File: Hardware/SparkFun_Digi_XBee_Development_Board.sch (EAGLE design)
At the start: 80 parts, among them J4 QWIIC_RIGHT_ANGLE, Q2 3.1A/30V/105mΩ, U1 FSUSB30MUX_MSOP10, U2 AP63203, U3 ESD Diode, U4 MCP73831, U5 ESD Diode, U7 FT231XS

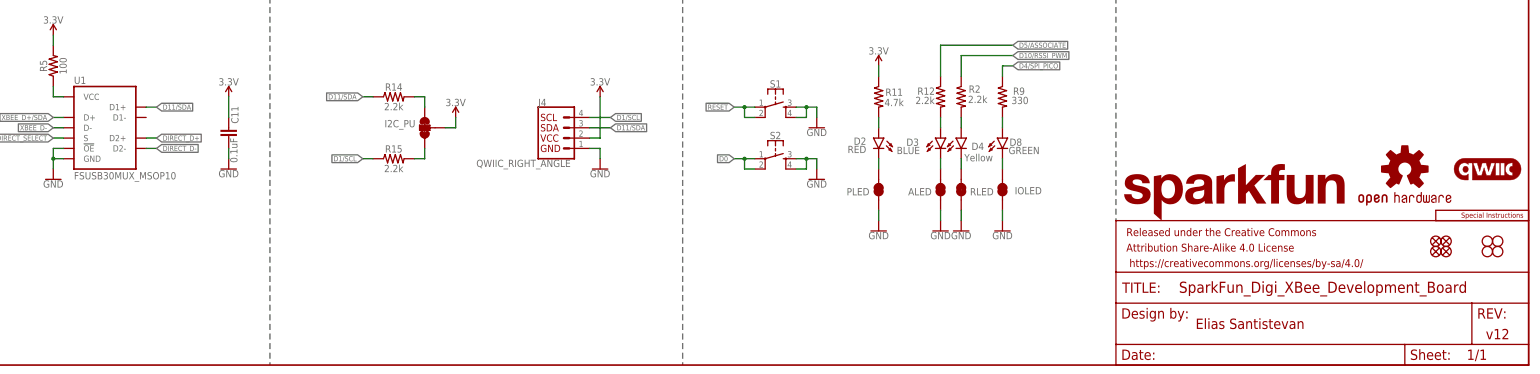
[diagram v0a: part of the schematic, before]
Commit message: Adds new FSUSB42 MUX switch
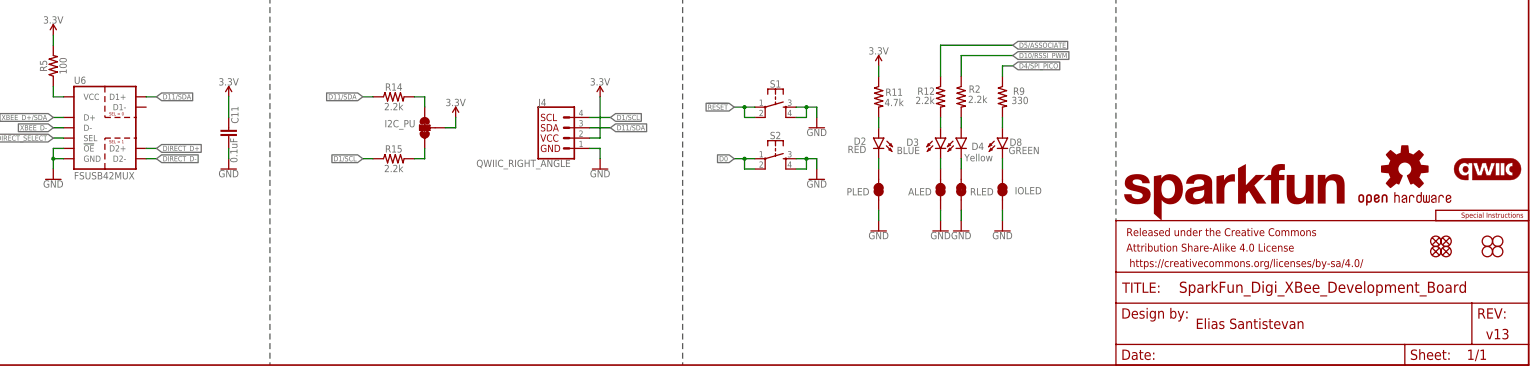
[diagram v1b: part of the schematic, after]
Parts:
- removed U1: FSUSB30MUX_MSOP10, SparkFun-IC-Special-Function:FSUSB30MUX_MSOP10
- added U6: FSUSB42MUX, SparkFun-IC-Special-Function:FSUSB42MUX
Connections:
- net D11/SDA: now also U6.D1+; no longer U1.D1+
- net DIRECT_D+: now also U6.D2+; no longer U1.D2+
- net DIRECT_D-: now also U6.D2-; no longer U1.D2-
- net DIRECT_SELECT: now also U6.SEL; no longer U1.S
- net GND: now also U6.!OE!, U6.GND; no longer U1.!OE!, U1.GND
- net N$3: now also U6.VCC; no longer U1.VCC
- net XBEE_D+/SDA: now also U6.D+; no longer U1.D+
- net XBEE_D-: now also U6.D-; no longer U1.D-
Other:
- note added: "v13"
- note removed: "v12"
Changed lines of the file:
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@@
 <part name="R12" library="SparkFun-Resistors" deviceset="2.2KOHM" device="-0603-1/10W-1%" value="2.2k"/>
 <part name="GND14" library="SparkFun-PowerSymbols" deviceset="GND" device=""/>
-<part name="U1" library="SparkFun-IC-Special-Function" deviceset="FSUSB30MUX" device="_MSOP10"/>
 <part name="GND22" library="SparkFun-PowerSymbols" deviceset="GND" device=""/>
 <part name="SUPPLY10" library="SparkFun-PowerSymbols" deviceset="3.3V" device=""/>
@@
 <part name="SUPPLY22" library="SparkFun-PowerSymbols" deviceset="V_USB" device=""/>
 <part name="SUPPLY6" library="SparkFun-PowerSymbols" deviceset="V_USB" device=""/>
+<part name="U6" library="SparkFun-IC-Special-Function" deviceset="FSUSB42MUX" device=""/>
 </parts>
 <sheets>
@@
 <wire x1="294.64" y1="187.96" x2="431.8" y2="187.96" width="0.2032" layer="97" style="longdash"/>
 <wire x1="121.92" y1="111.76" x2="121.92" y2="0" width="0.2032" layer="97" style="longdash"/>
-<text x="424.18" y="7.62" size="2.54" layer="94" font="vector" align="center">v12</text>
+<text x="424.18" y="7.62" size="2.54" layer="94" font="vector" align="center">v13</text>
 <text x="363.22" y="10.16" size="2.54" layer="94" font="vector" align="center">Elias Santistevan</text>
 <wire x1="223.52" y1="111.76" x2="223.52" y2="0" width="0.2032" layer="97" style="longdash"/>
@@
 <attribute name="VALUE" x="287.02" y="32.766" size="1.778" layer="96" font="vector" align="top-center"/>
 </instance>
-<instance part="U1" gate="U1" x="81.28" y="58.42" smashed="yes">
-<attribute name="NAME" x="73.66" y="69.215" size="1.778" layer="95" font="vector"/>
-<attribute name="VALUE" x="73.66" y="45.72" size="1.778" layer="96" font="vector"/>
-</instance>
 <instance part="GND22" gate="1" x="17.78" y="210.82" smashed="yes" rot="MR0">
 <attribute name="VALUE" x="17.78" y="210.566" size="1.778" layer="96" font="vector" rot="MR0" align="top-center"/>
@@
 <attribute name="VALUE" x="353.06" y="246.634" size="1.778" layer="96" font="vector" align="bottom-center"/>
 </instance>
+<instance part="U6" gate="G$1" x="81.28" y="58.42" smashed="yes">
+<attribute name="NAME" x="73.66" y="69.215" size="1.778" layer="95" font="vector"/>
+<attribute name="VALUE" x="73.66" y="45.72" size="1.778" layer="96" font="vector"/>
+</instance>
 </instances>
 <busses>
@@
 </segment>
 <segment>
-<pinref part="U1" gate="U1" pin="D1+"/>
-<wire x1="93.98" y1="63.5" x2="91.44" y2="63.5" width="0.1524" layer="91"/>
-<label x="93.98" y="63.5" size="1.27" layer="95" font="vector" xref="yes"/>
+<wire x1="93.98" y1="66.04" x2="91.44" y2="66.04" width="0.1524" layer="91"/>
+<label x="93.98" y="66.04" size="1.27" layer="95" font="vector" xref="yes"/>
+<pinref part="U6" gate="G$1" pin="D1+"/>
 </segment>
 <segment>
@@
 </segment>
 <segment>
-<pinref part="U1" gate="U1" pin="GND"/>
 <wire x1="68.58" y1="48.26" x2="68.58" y2="50.8" width="0.1524" layer="91"/>
 <wire x1="68.58" y1="50.8" x2="71.12" y2="50.8" width="0.1524" layer="91"/>
 <pinref part="GND29" gate="1" pin="GND"/>
-<pinref part="U1" gate="U1" pin="!OE!"/>
 <wire x1="71.12" y1="53.34" x2="68.58" y2="53.34" width="0.1524" layer="91"/>
 <wire x1="68.58" y1="53.34" x2="68.58" y2="50.8" width="0.1524" layer="91"/>
 <junction x="68.58" y="50.8"/>
+<pinref part="U6" gate="G$1" pin="GND"/>
+<pinref part="U6" gate="G$1" pin="!OE!"/>
 </segment>
 <segment>
@@
 </segment>
 <segment>
-<pinref part="U1" gate="U1" pin="D+"/>
 <wire x1="68.58" y1="60.96" x2="71.12" y2="60.96" width="0.1524" layer="91"/>
 <label x="68.58" y="60.96" size="1.27" layer="95" font="vector" rot="R180" xref="yes"/>
+<pinref part="U6" gate="G$1" pin="D+"/>
 </segment>
 </net>
@@
 </segment>
 <segment>
-<pinref part="U1" gate="U1" pin="D-"/>
 <wire x1="68.58" y1="58.42" x2="71.12" y2="58.42" width="0.1524" layer="91"/>
 <label x="68.58" y="58.42" size="1.27" layer="95" font="vector" rot="R180" xref="yes"/>
+<pinref part="U6" gate="G$1" pin="D-"/>
 </segment>
 </net>
 <net name="DIRECT_D+" class="2">
 <segment>
-<pinref part="U1" gate="U1" pin="D2+"/>
-<wire x1="93.98" y1="55.88" x2="91.44" y2="55.88" width="0.1524" layer="91"/>
-<label x="93.98" y="55.88" size="1.27" layer="95" font="vector" xref="yes"/>
+<wire x1="93.98" y1="53.34" x2="91.44" y2="53.34" width="0.1524" layer="91"/>
+<label x="93.98" y="53.34" size="1.27" layer="95" font="vector" xref="yes"/>
+<pinref part="U6" gate="G$1" pin="D2+"/>
 </segment>
 <segment>
@@
 <net name="DIRECT_D-" class="2">
 <segment>
-<pinref part="U1" gate="U1" pin="D2-"/>
-<wire x1="93.98" y1="53.34" x2="91.44" y2="53.34" width="0.1524" layer="91"/>
-<label x="93.98" y="53.34" size="1.27" layer="95" font="vector" xref="yes"/>
+<wire x1="93.98" y1="50.8" x2="91.44" y2="50.8" width="0.1524" layer="91"/>
+<label x="93.98" y="50.8" size="1.27" layer="95" font="vector" xref="yes"/>
+<pinref part="U6" gate="G$1" pin="D2-"/>
 </segment>
 <segment>
@@
 <net name="DIRECT_SELECT" class="0">
 <segment>
-<pinref part="U1" gate="U1" pin="S"/>
 <wire x1="71.12" y1="55.88" x2="68.58" y2="55.88" width="0.1524" layer="91"/>
 <label x="68.58" y="55.88" size="1.27" layer="95" font="vector" rot="R180" xref="yes"/>
+<pinref part="U6" gate="G$1" pin="SEL"/>
 </segment>
 <segment>
@@
 <net name="N$3" class="0">
 <segment>
-<pinref part="U1" gate="U1" pin="VCC"/>
 <pinref part="R5" gate="G$1" pin="1"/>
 <wire x1="71.12" y1="66.04" x2="68.58" y2="66.04" width="0.1524" layer="91"/>
 <wire x1="68.58" y1="66.04" x2="68.58" y2="68.58" width="0.1524" layer="91"/>
-</segment>
-</net>
+<pinref part="U6" gate="G$1" pin="VCC"/>
+</segment>
+</net>

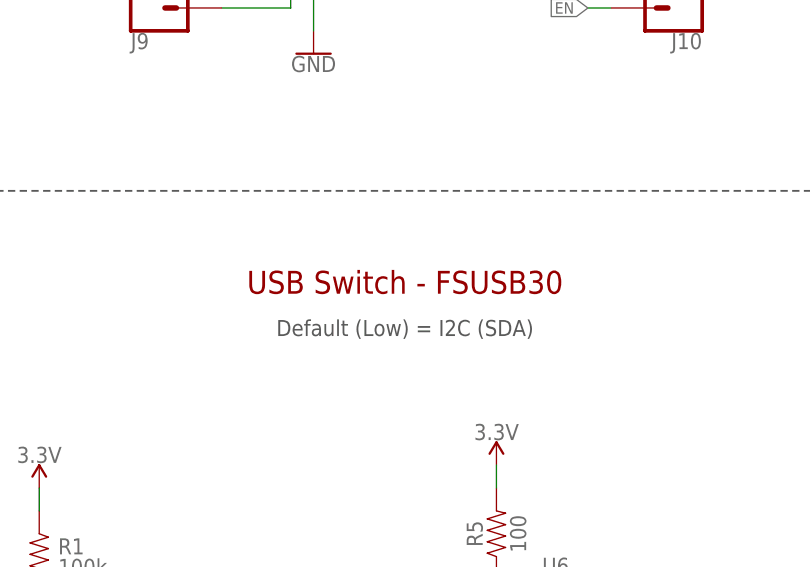
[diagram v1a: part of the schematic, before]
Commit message: Update to schematic text
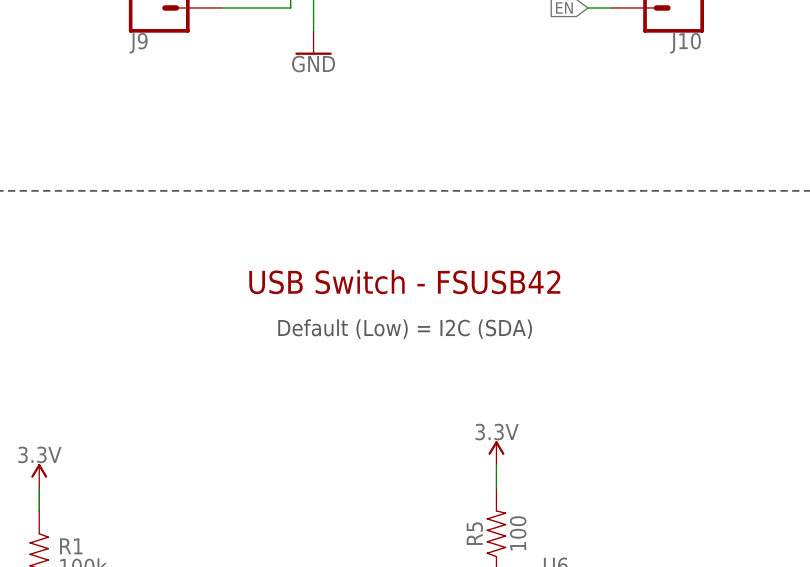
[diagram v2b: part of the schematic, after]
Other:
- note added: "USB Switch - FSUSB42"
- note removed: "USB Switch - FSUSB30"
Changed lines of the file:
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@@
 <text x="363.22" y="10.16" size="2.54" layer="94" font="vector" align="center">Elias Santistevan</text>
 <wire x1="223.52" y1="111.76" x2="223.52" y2="0" width="0.2032" layer="97" style="longdash"/>
-<text x="58.42" y="101.6" size="2.54" layer="94" font="vector" align="center">USB Switch - FSUSB30</text>
+<text x="58.42" y="101.6" size="2.54" layer="94" font="vector" align="center">USB Switch - FSUSB42</text>
 <text x="58.42" y="96.52" size="1.778" layer="97" font="vector" align="center">Default (Low) = I2C (SDA)</text>
 <wire x1="330.2" y1="111.76" x2="330.2" y2="35.56" width="0.2032" layer="97" style="longdash"/>

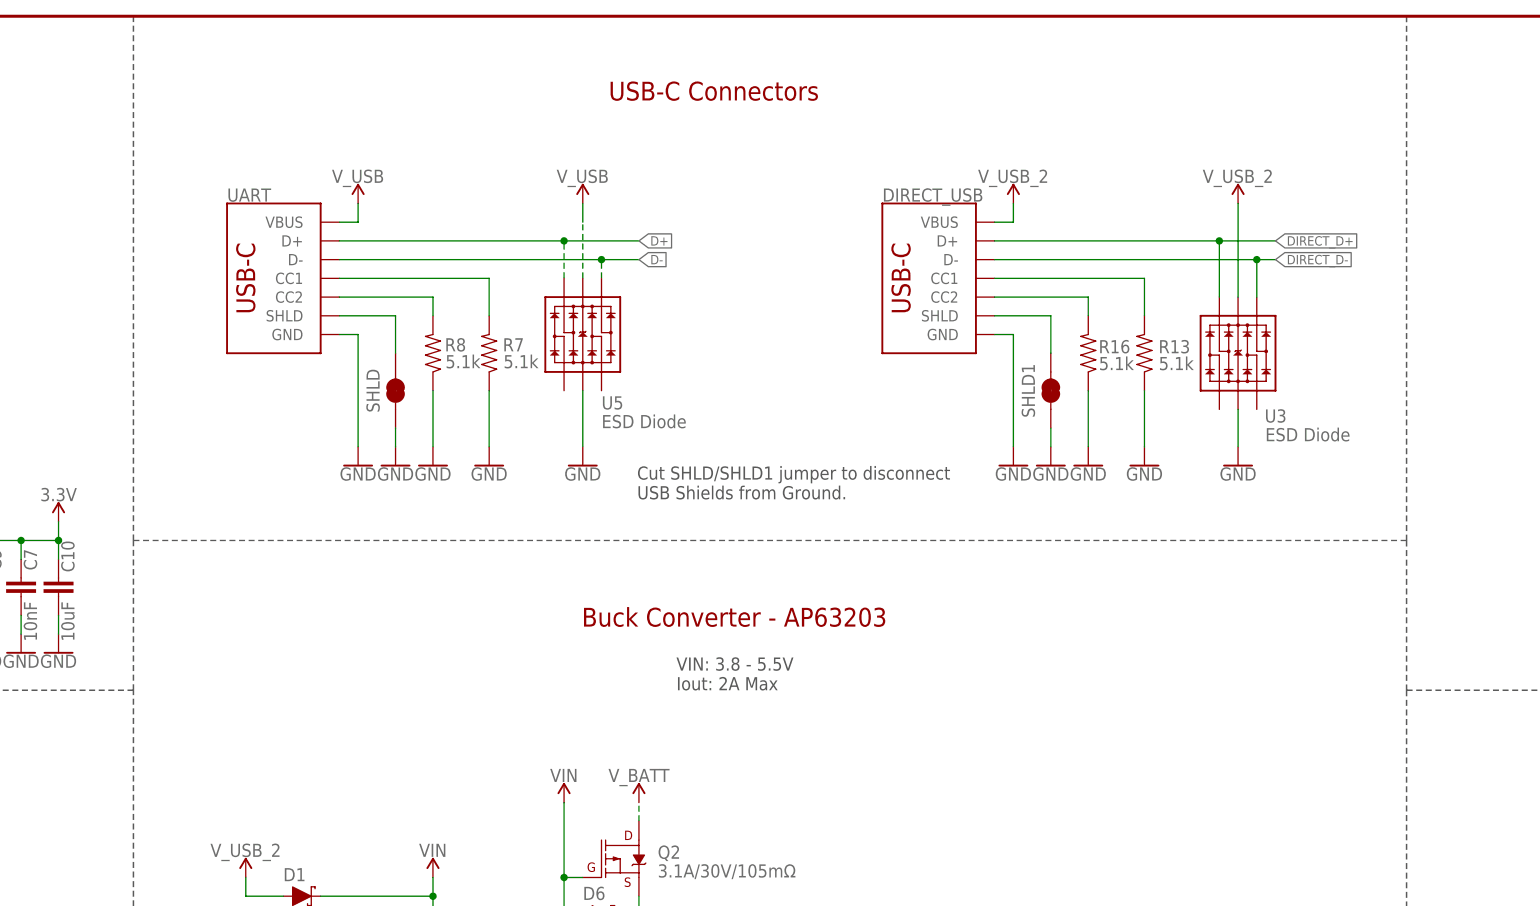
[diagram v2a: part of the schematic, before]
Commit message: Adds text for USB calculation, nudges some things around for better pour
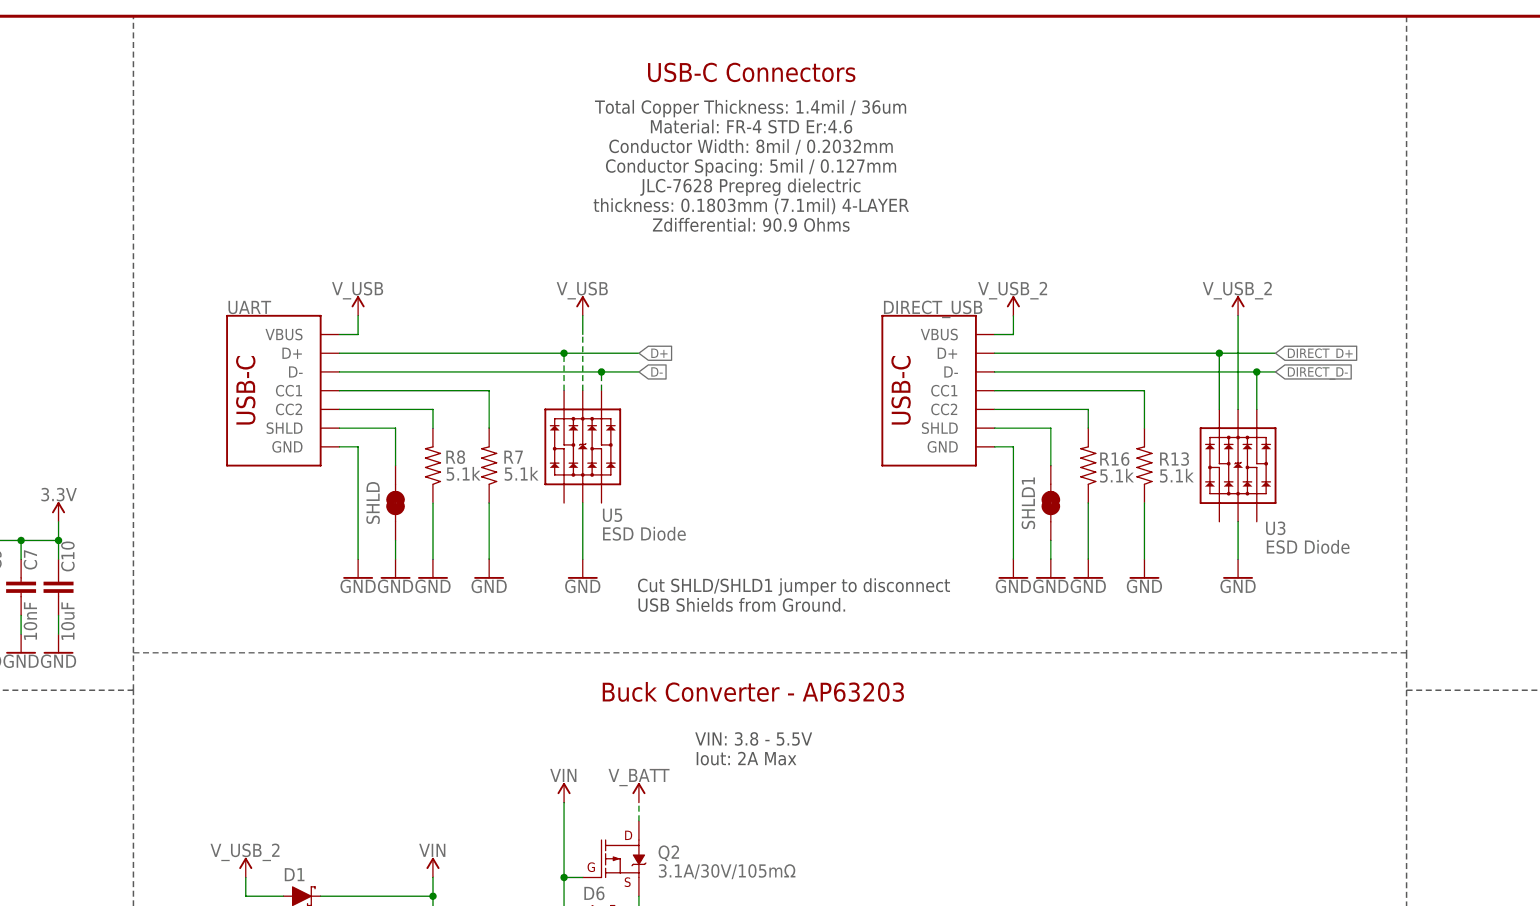
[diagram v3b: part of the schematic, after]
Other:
- note added: "Total Copper Thickness: 1.4mil / 36um Material: FR-4 STD Er:4.6 Conductor Width: 8mil / 0.2032mm Conductor Spacing: 5mil / 0.127mm JLC-7628 Prepreg dielectric thickness: 0.1803mm (7.1mil) 4-LAYER Zdifferential: 90.9 Ohms"
- moved on the sheet: DIRECT_USB, R13, R16, R7, R8, SHLD, SHLD1, U3, U5, UART

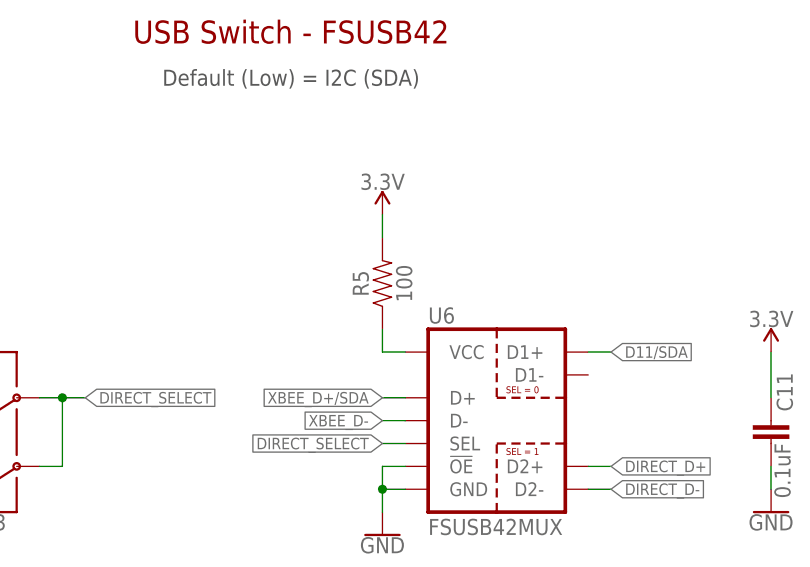
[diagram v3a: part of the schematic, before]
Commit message: Moves from 100 OHm to 0 OHm on VCC input for FUSB42
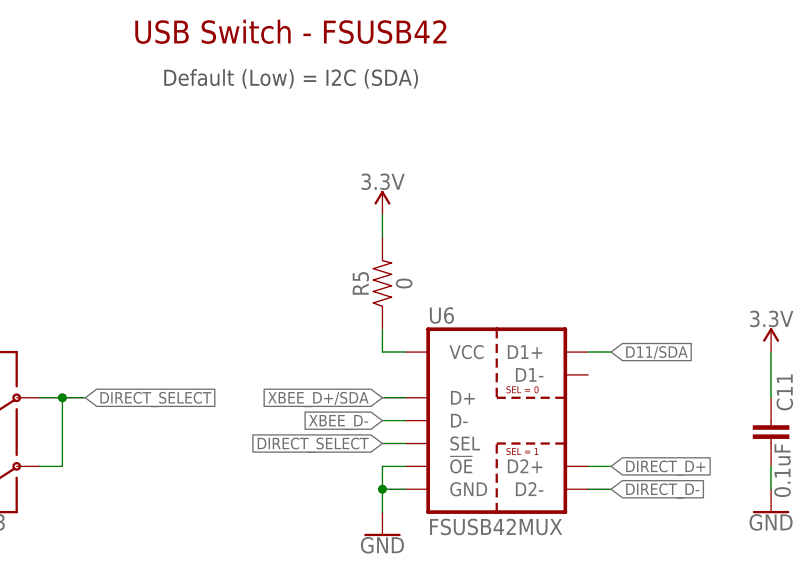
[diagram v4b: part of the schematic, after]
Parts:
- R5: value 100 -> 0; device SparkFun-Resistors:100OHM-0603-1/10W-1% -> SparkFun-Resistors:0OHM-0603-1/10W
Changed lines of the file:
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@@
 <part name="GND8" library="SparkFun-PowerSymbols" deviceset="GND" device=""/>
 <part name="SUPPLY24" library="SparkFun-PowerSymbols" deviceset="3.3V" device=""/>
-<part name="R5" library="SparkFun-Resistors" deviceset="100OHM" device="-0603-1/10W-1%" value="100"/>
+<part name="R5" library="SparkFun-Resistors" deviceset="0OHM" device="-0603-1/10W" value="0"/>
 <part name="C12" library="SparkFun-Capacitors" deviceset="10PF" device="-0603-50V-5%" value="10pF"/>
 <part name="C13" library="SparkFun-Capacitors" deviceset="47PF" device="-0603-50V-5%" value="47pF"/>
